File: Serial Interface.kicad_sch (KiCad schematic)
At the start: 28 parts

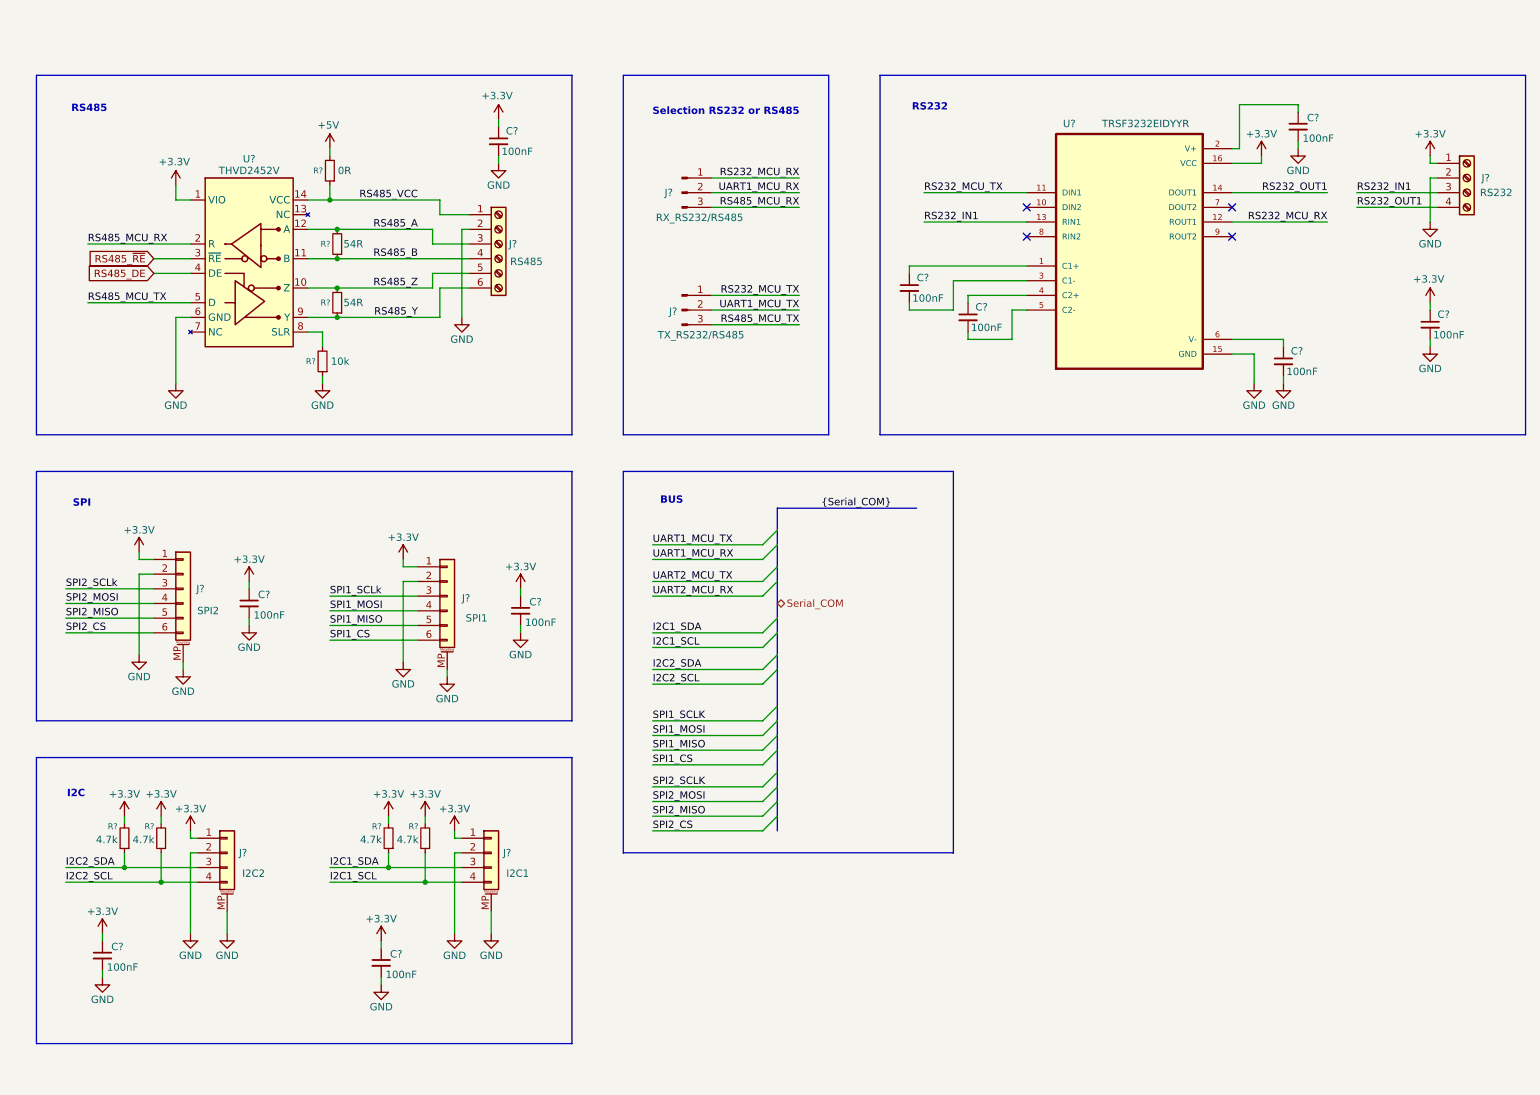
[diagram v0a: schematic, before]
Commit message: Add IOT Part
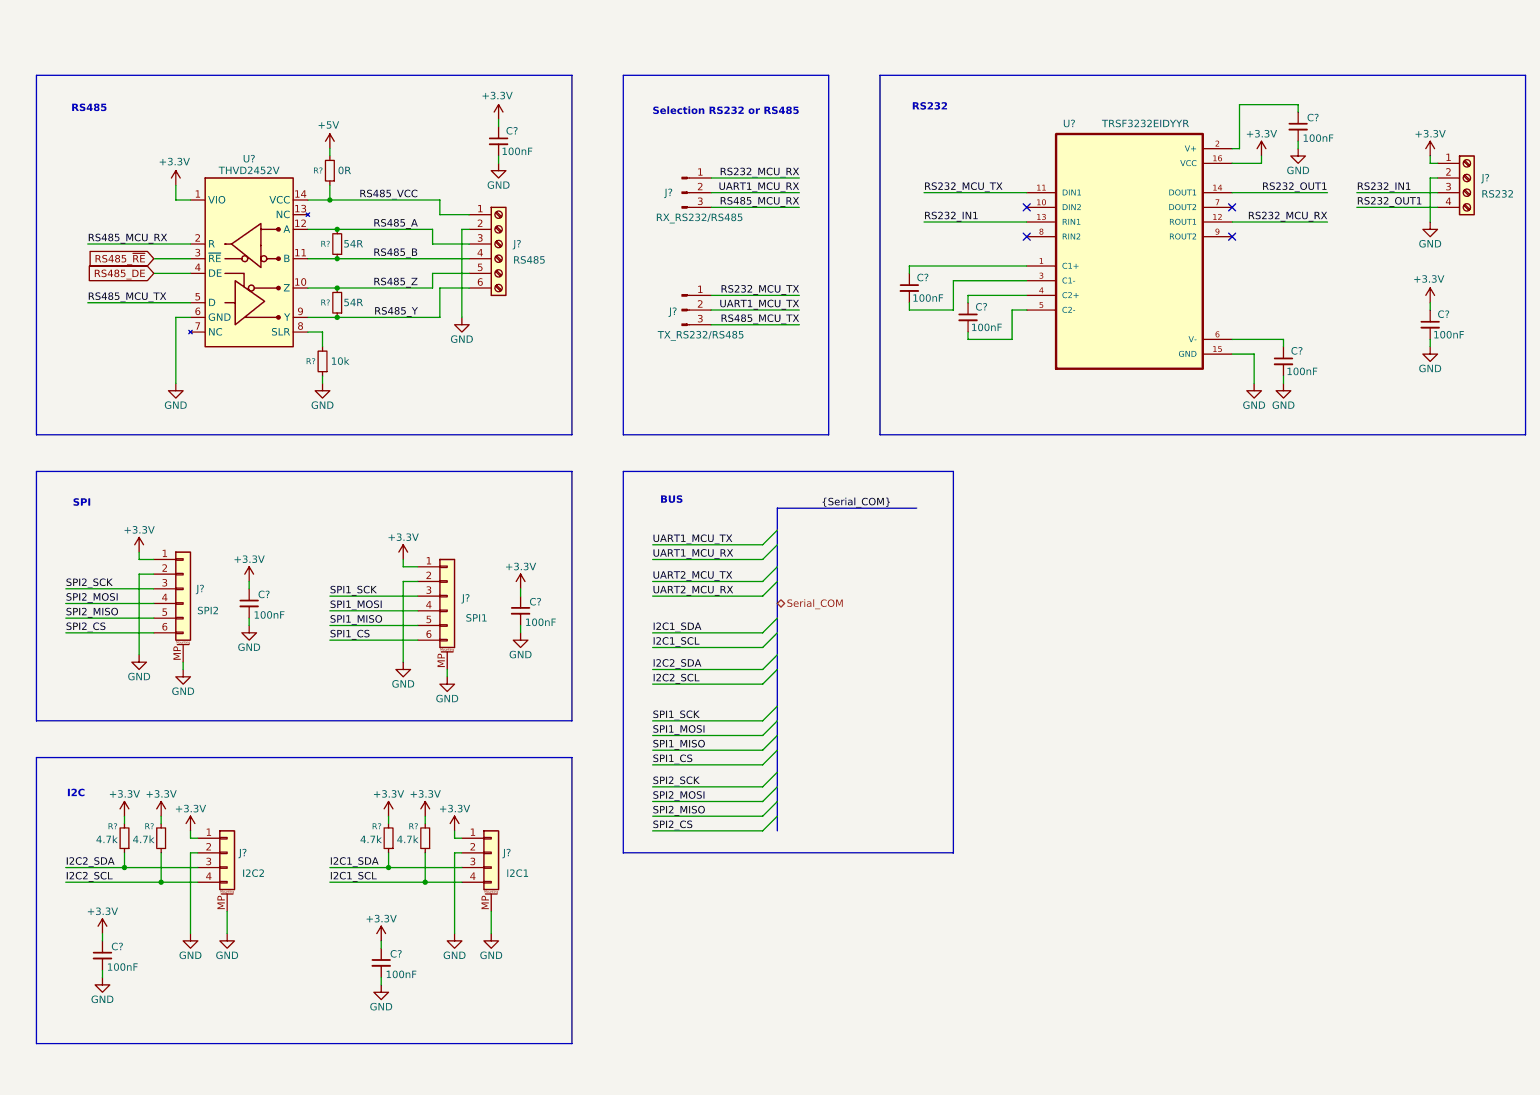
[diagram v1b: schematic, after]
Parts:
- removed J?: *, TerminalBlock_Phoenix:TerminalBlock_Phoenix_MPT-0,5-4-2.54_1x04_P2.54mm_Horizontal, symbol Connector:Screw_Terminal_01x04
- removed J?: *, TerminalBlock_Phoenix:TerminalBlock_Phoenix_MPT-0,5-6-2.54_1x06_P2.54mm_Horizontal, symbol Connector:Screw_Terminal_01x06
- added J?: *, TerminalBlock_Phoenix:TerminalBlock_Phoenix_MKDS-1,5-6-5.08_1x06_P5.08mm_Horizontal, symbol Connector:Screw_Terminal_01x06
- added J?: *, TerminalBlock_Phoenix:TerminalBlock_Phoenix_MKDS-1,5-4-5.08_1x04_P5.08mm_Horizontal, symbol Connector:Screw_Terminal_01x04
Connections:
- net +3.3V: now also J?.1 (Pin_1)
- net GND: now also J?.2 (Pin_2), J?.2 (Pin_2)
- net RS232_IN1: now also J?.3 (Pin_3)
- net RS232_OUT1: now also J?.4 (Pin_4)
- net RS485_A: now also J?.3 (Pin_3)
- net RS485_B: now also J?.4 (Pin_4)
- net RS485_VCC: now also J?.1 (Pin_1)
- net RS485_Y: now also J?.6 (Pin_6)
- net RS485_Z: now also J?.5 (Pin_5)
- net SPI1_SCLk renamed SPI1_SCK
- net SPI2_SCLk renamed SPI2_SCK

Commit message: IoT part finalization
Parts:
- added C?: 100nF, Capacitor_SMD:C_0603_1608Metric_Pad1.08x0.95mm_HandSolder, symbol Device:C_Small
- added J?: *, Connector_JST:JST_PH_S4B-PH-SM4-TB_1x04-1MP_P2.00mm_Horizontal, symbol Connector_Generic_MountingPin:Conn_01x04_MountingPin
- added R? (x2): 4.7k, Resistor_SMD:R_0603_1608Metric_Pad0.98x0.95mm_HandSolder, symbol Device:R_Small
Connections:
- net +3.3V: now also C?.1, J?.1 (Pin_1), R?.2, R?.2
- net GND: now also C?.2, J?.2 (Pin_2), J?.MP (MountPin)
- net UART1_MCU_RX renamed RS_UART_MCU_RX
- net UART1_MCU_TX renamed RS_UART_MCU_TX
- new net I2C3_SCL: J?.4 (Pin_4), R?.1
- new net I2C3_SDA: J?.3 (Pin_3), R?.1
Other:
- moved on the sheet: C?, J?, R?

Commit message: IOT part Finilization
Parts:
- added C?: 100nF, Capacitor_SMD:C_0603_1608Metric_Pad1.08x0.95mm_HandSolder, symbol Device:C_Small
- added J?: *, Connector_JST:JST_PH_S4B-PH-SM4-TB_1x04-1MP_P2.00mm_Horizontal, symbol Connector_Generic_MountingPin:Conn_01x04_MountingPin
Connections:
- net +3.3V: now also C?.1, J?.1 (Pin_1)
- net GND: now also C?.2, J?.2 (Pin_2), J?.MP (MountPin)
- new net UART2_MCU_RX: J?.4 (Pin_4)
- new net UART2_MCU_TX: J?.3 (Pin_3)
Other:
- note added: "UART"

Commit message: Release Schematic REV A-01
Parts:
- gave numbers to parts that had none: 34
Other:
- company: Blue Signal -> Nexvantis
- moved on the sheet: C38, C39

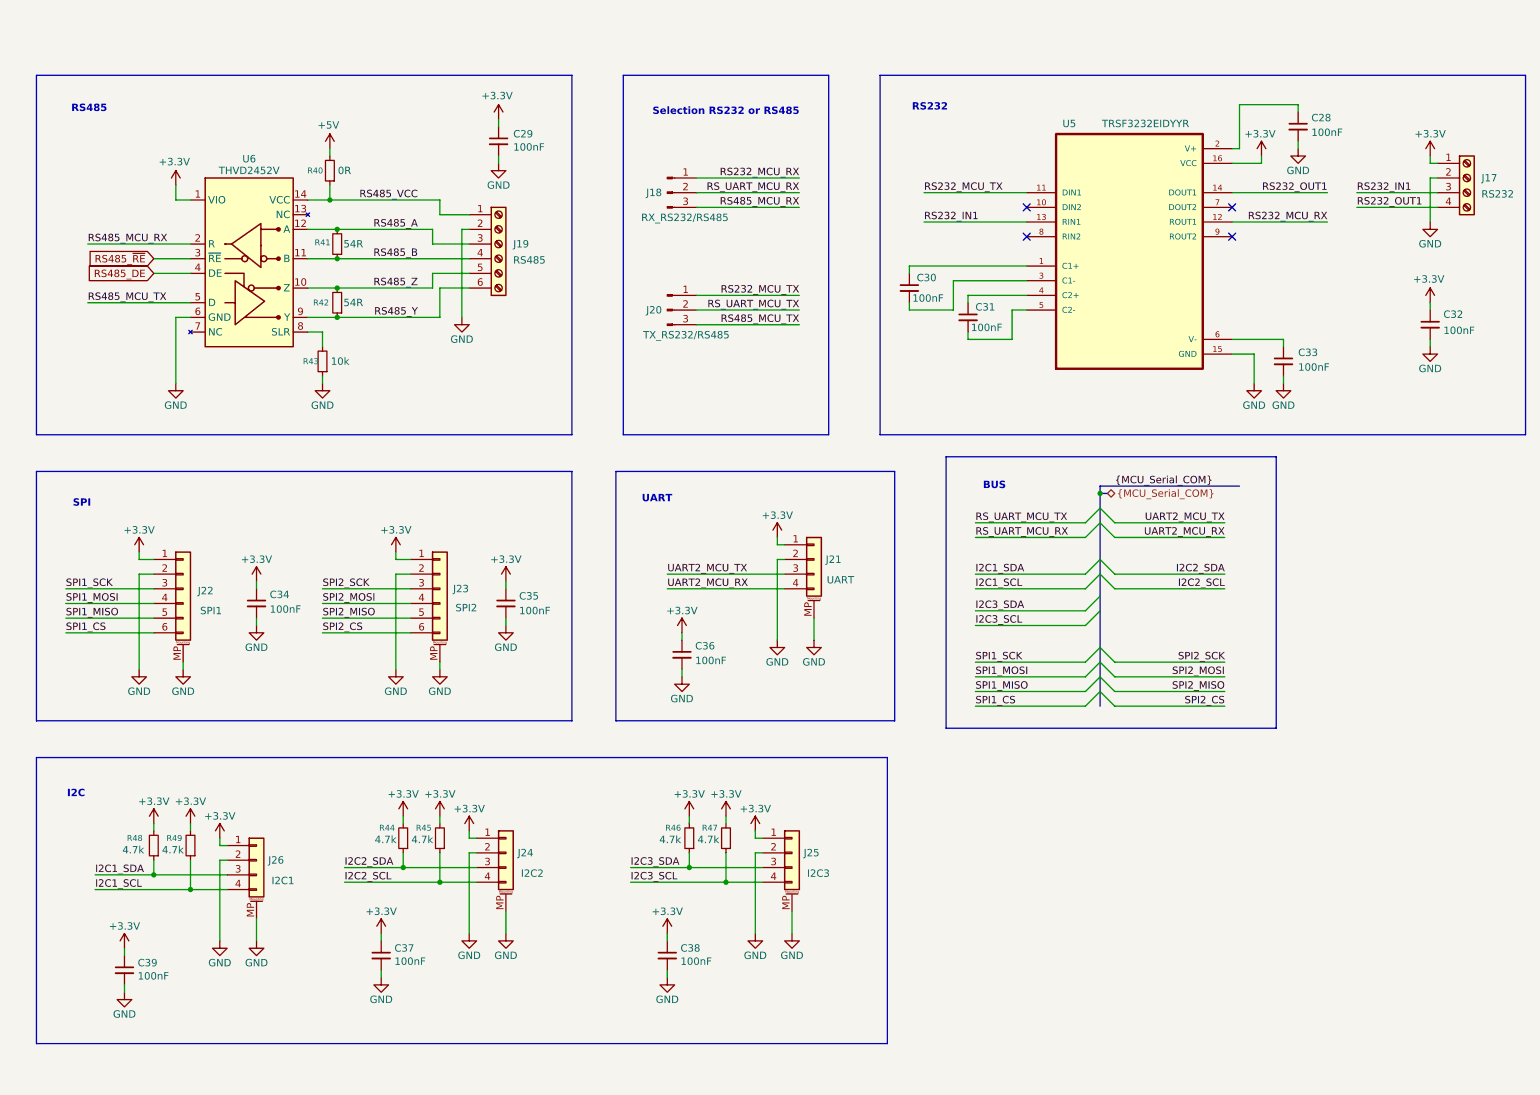
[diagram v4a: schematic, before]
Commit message: [Project][Added] CI/CD environment
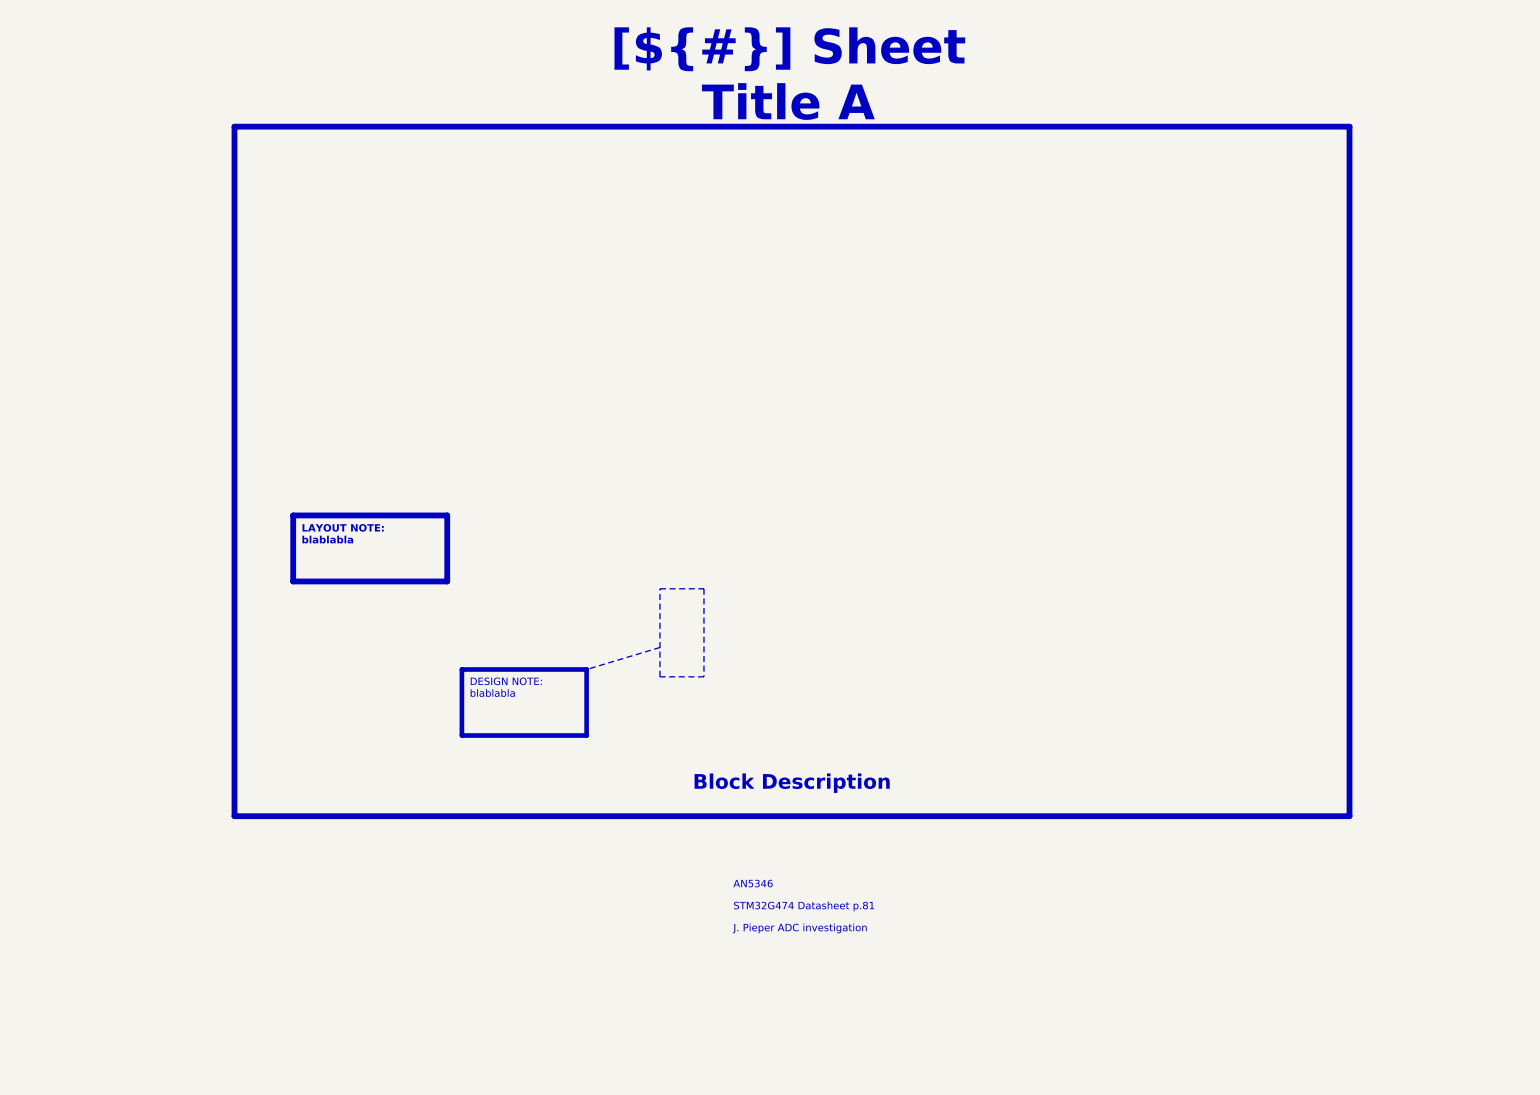
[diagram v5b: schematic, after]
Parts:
- removed C28, C29, C30, C31, C32, C33, C34, C35, C36, C37, C38, C39: 100nF, Capacitor_SMD:C_0603_1608Metric_Pad1.08x0.95mm_HandSolder, symbol Device:C_Small
- removed J17: *, TerminalBlock_Phoenix:TerminalBlock_Phoenix_MKDS-1,5-4-5.08_1x04_P5.08mm_Horizontal, symbol Connector:Screw_Terminal_01x04
- removed J18, J20: *, Connector_PinHeader_2.54mm:PinHeader_1x03_P2.54mm_Vertical, symbol Connector:Conn_01x03_Pin
- removed J19: *, TerminalBlock_Phoenix:TerminalBlock_Phoenix_MKDS-1,5-6-5.08_1x06_P5.08mm_Horizontal, symbol Connector:Screw_Terminal_01x06
- removed J21, J24, J25, J26: *, Connector_JST:JST_PH_S4B-PH-SM4-TB_1x04-1MP_P2.00mm_Horizontal, symbol Connector_Generic_MountingPin:Conn_01x04_MountingPin
- removed J22, J23: *, Connector_JST:JST_PH_S6B-PH-SM4-TB_1x06-1MP_P2.00mm_Horizontal, symbol Connector_Generic_MountingPin:Conn_01x06_MountingPin
- removed R40: 0R, Resistor_SMD:R_0603_1608Metric_Pad0.98x0.95mm_HandSolder, symbol Device:R_Small
- removed R41, R42: 54R, Resistor_SMD:R_0603_1608Metric_Pad0.98x0.95mm_HandSolder, symbol Device:R_Small
- removed R43: 10k, Resistor_SMD:R_0603_1608Metric_Pad0.98x0.95mm_HandSolder, symbol Device:R_Small
- removed R44, R45, R46, R47, R48, R49: 4.7k, Resistor_SMD:R_0603_1608Metric_Pad0.98x0.95mm_HandSolder, symbol Device:R_Small
- removed U5: *, Package_SO:Texas_DYY0016A_TSOT-23-16_2x4.2mm_P0.5mm, symbol P_Interface:TRSF3232EIDYYR
- removed U6: *, Package_SO:SOIC-14_3.9x8.7mm_P1.27mm, symbol P_Interface:THVD2452V
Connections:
- no-connect marks 4 -> 0
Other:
- note added: "AN5346"
- note added: "J. Pieper ADC investigation"
- note added: "STM32G474 Datasheet p.81"
- note removed: "BUS"
- note removed: "I2C"
- note removed: "RS232"
- note removed: "RS485"
- note removed: "SPI"
- note removed: "Selection RS232 or RS485"
- note removed: "UART"
- company: Nexvantis -> ${COMPANY}
- title: Data Acquisition Board -> Sheet Title A
